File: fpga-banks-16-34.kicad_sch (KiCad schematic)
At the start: 25 parts, among them U1 ASFLMB-100.000MHZ-XY-T, U15 XC7K160T-FFG676, U8 PCA9517ADMR2G

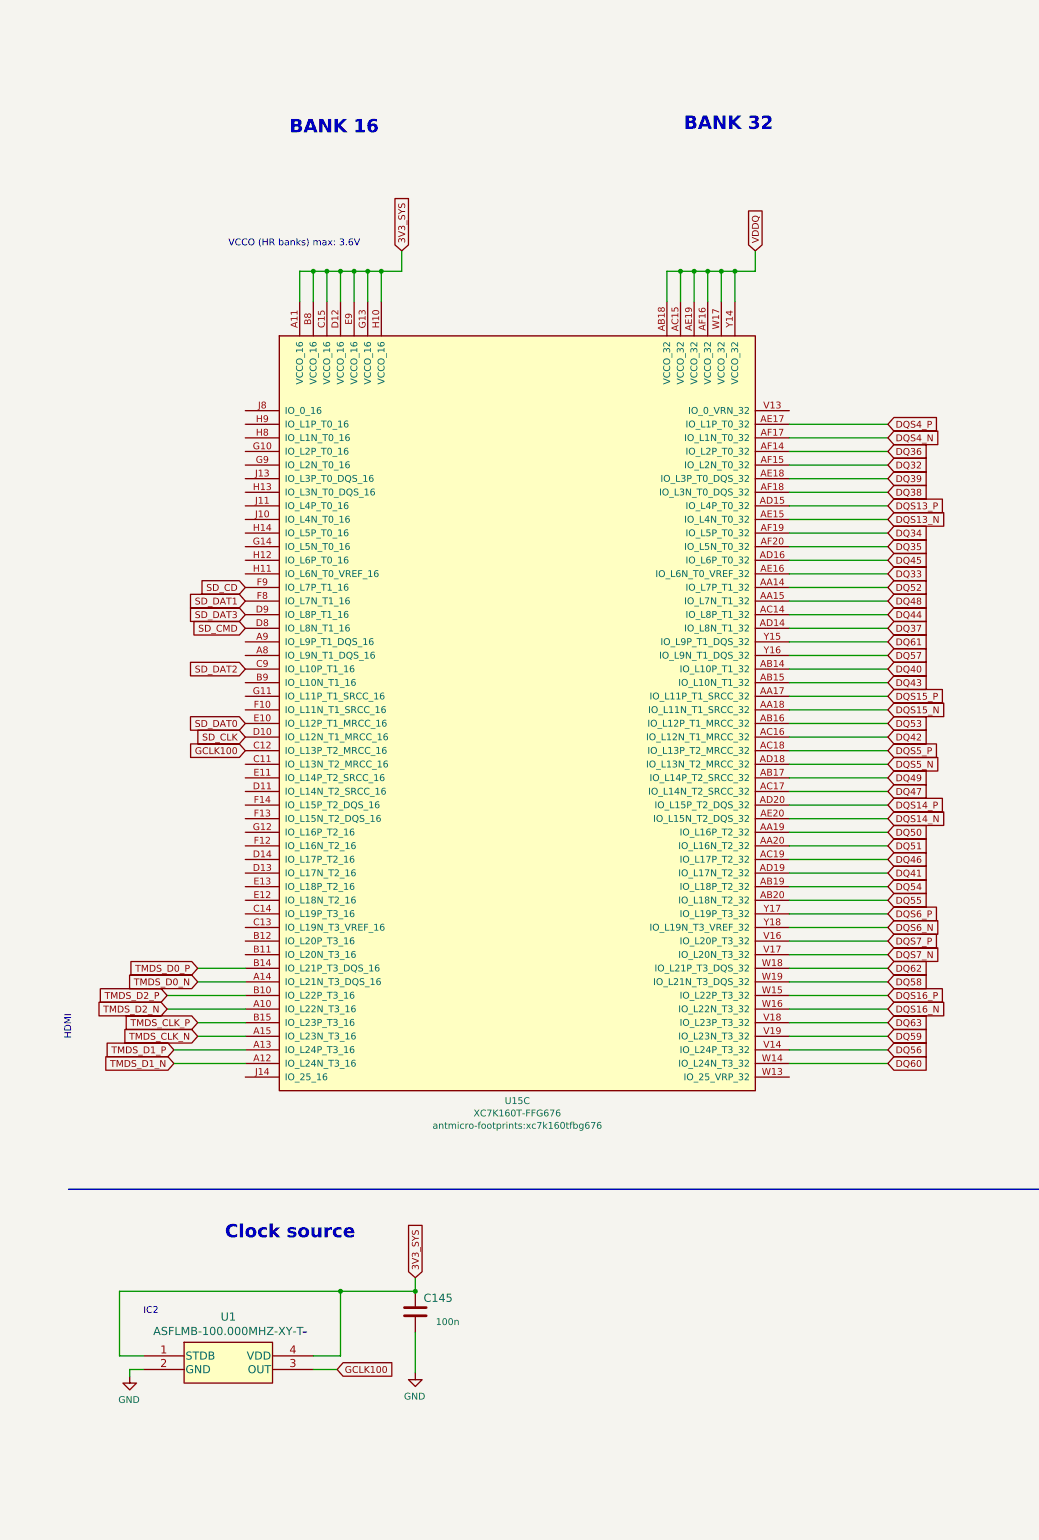
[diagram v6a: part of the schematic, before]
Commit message: Add missing FMC vias, route: MODE, JTAG, active discharge, reconnect 5V buses
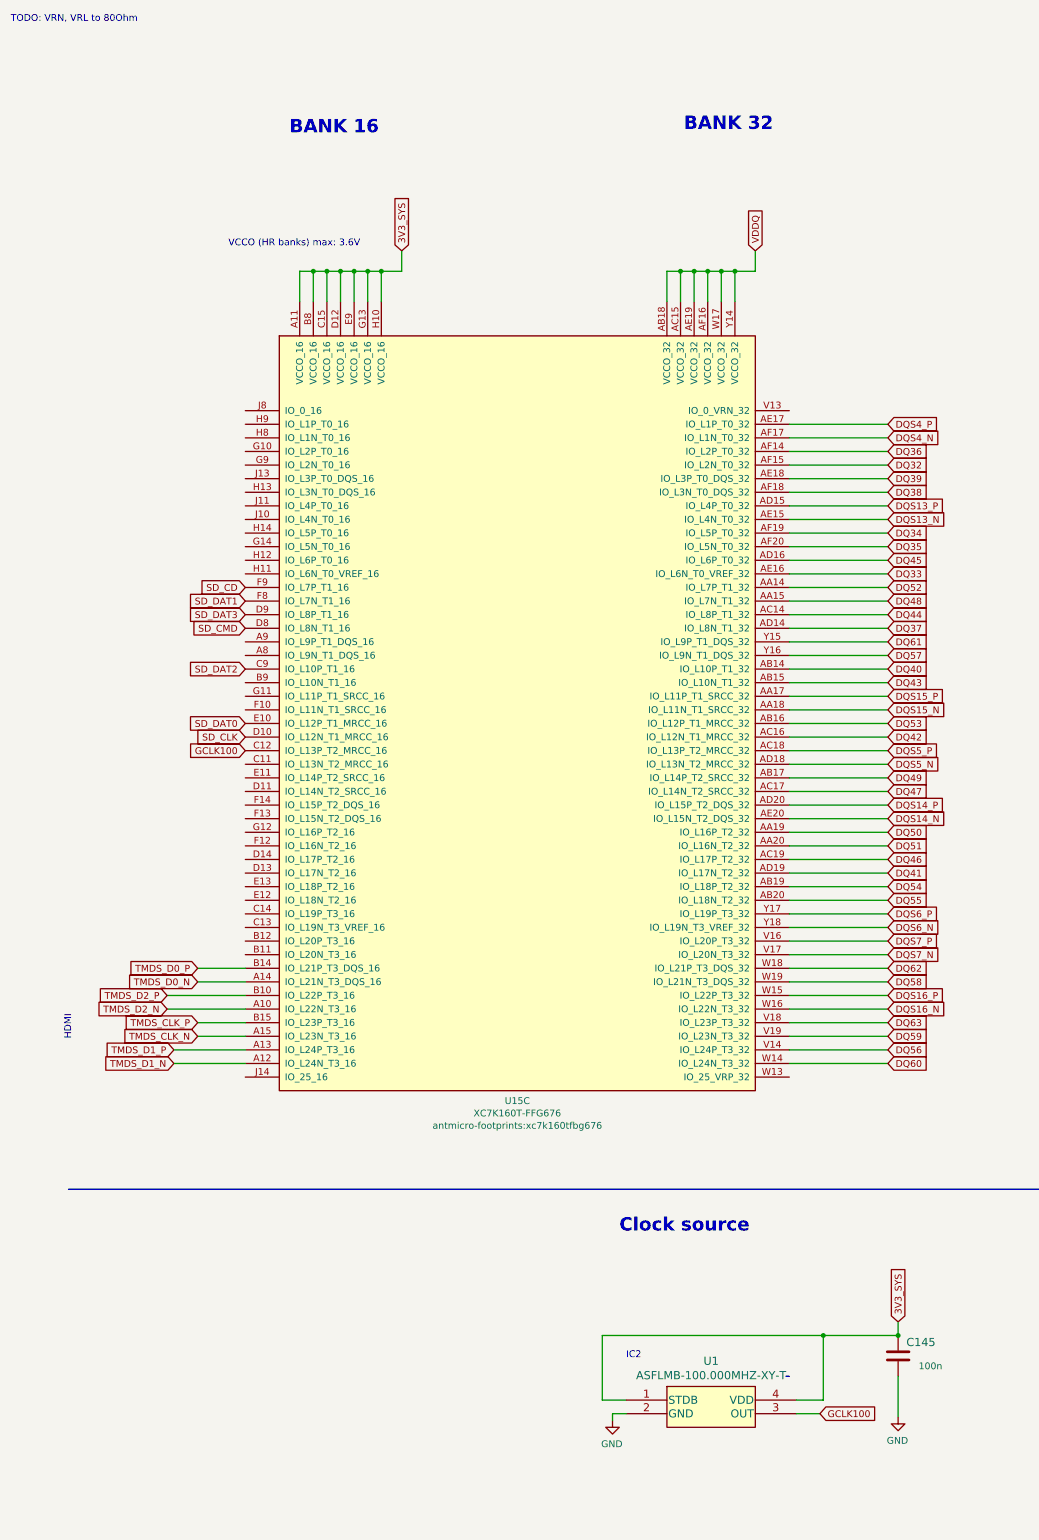
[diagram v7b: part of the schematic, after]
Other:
- note added: "TODO: VRN, VRL to 80Ohm"
- moved on the sheet: C145, U1
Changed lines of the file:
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@@
   (junction (at 60.96 50.165) (diameter 0) (color 0 0 0 0)
   )
-  (junction (at 77.47 240.665) (diameter 0) (color 0 0 0 0)
+  (junction (at 167.64 248.92) (diameter 0) (color 0 0 0 0)
   )
   (junction (at 278.13 262.89) (diameter 0) (color 0 0 0 0)
@@
   (junction (at 264.795 53.34) (diameter 0) (color 0 0 0 0)
   )
-  (junction (at 63.5 240.665) (diameter 0) (color 0 0 0 0)
+  (junction (at 153.67 248.92) (diameter 0) (color 0 0 0 0)
   )
   (junction (at 134.62 50.165) (diameter 0) (color 0 0 0 0)
@@
     (stroke (width 0) (type default) (color 0 0 0 0))
   )
-  (wire (pts (xy 58.42 255.27) (xy 62.865 255.27))
+  (wire (pts (xy 148.59 263.525) (xy 153.035 263.525))
     (stroke (width 0) (type default) (color 0 0 0 0))
   )
@@
     (stroke (width 0) (type default) (color 0 0 0 0))
   )
-  (wire (pts (xy 77.47 248.285) (xy 77.47 255.905))
+  (wire (pts (xy 167.64 256.54) (xy 167.64 264.16))
     (stroke (width 0) (type default) (color 0 0 0 0))
   )
@@
     (stroke (width 0) (type default) (color 0 0 0 0))
   )
-  (wire (pts (xy 22.225 240.665) (xy 63.5 240.665))
+  (wire (pts (xy 112.395 248.92) (xy 153.67 248.92))
     (stroke (width 0) (type default) (color 0 0 0 0))
   )
@@
     (stroke (width 0) (type default) (color 0 0 0 0))
   )
-  (wire (pts (xy 58.42 252.73) (xy 63.5 252.73))
+  (wire (pts (xy 148.59 260.985) (xy 153.67 260.985))
     (stroke (width 0) (type default) (color 0 0 0 0))
   )
-  (wire (pts (xy 26.67 255.27) (xy 24.13 255.27))
+  (wire (pts (xy 116.84 263.525) (xy 114.3 263.525))
     (stroke (width 0) (type default) (color 0 0 0 0))
   )
@@
     (stroke (width 0) (type default) (color 0 0 0 0))
   )
-  (wire (pts (xy 22.225 240.665) (xy 22.225 252.73))
+  (wire (pts (xy 112.395 248.92) (xy 112.395 260.985))
     (stroke (width 0) (type default) (color 0 0 0 0))
   )
@@
     (stroke (width 0) (type default) (color 0 0 0 0))
   )
-  (wire (pts (xy 24.13 255.27) (xy 24.13 256.54))
+  (wire (pts (xy 114.3 263.525) (xy 114.3 264.795))
     (stroke (width 0) (type default) (color 0 0 0 0))
   )
@@
     (stroke (width 0) (type default) (color 0 0 0 0))
   )
-  (wire (pts (xy 63.5 240.665) (xy 77.47 240.665))
+  (wire (pts (xy 153.67 248.92) (xy 167.64 248.92))
     (stroke (width 0) (type default) (color 0 0 0 0))
   )
@@
     (stroke (width 0) (type default) (color 0 0 0 0))
   )
-  (polyline (pts (xy 56.515 248.285) (xy 57.15 248.285))
+  (polyline (pts (xy 146.685 256.54) (xy 147.32 256.54))
     (stroke (width 0) (type default) (color 0 0 0 0))
   )
@@
     (stroke (width 0) (type default) (color 0 0 0 0))
   )
-  (wire (pts (xy 22.225 252.73) (xy 26.67 252.73))
+  (wire (pts (xy 112.395 260.985) (xy 116.84 260.985))
     (stroke (width 0) (type default) (color 0 0 0 0))
   )
@@
     (stroke (width 0) (type default) (color 0 0 0 0))
   )
-  (wire (pts (xy 77.47 240.665) (xy 77.47 238.125))
+  (wire (pts (xy 167.64 248.92) (xy 167.64 246.38))
     (stroke (width 0) (type default) (color 0 0 0 0))
   )
@@
     (stroke (width 0) (type default) (color 0 0 0 0))
   )
-  (wire (pts (xy 63.5 252.73) (xy 63.5 240.665))
+  (wire (pts (xy 153.67 260.985) (xy 153.67 248.92))
     (stroke (width 0) (type default) (color 0 0 0 0))
   )
@@
     (effects (font (size 2.4892 2.4892) (thickness 0.4978) bold) (justify left bottom))
   )
-  (text "Clock source" (at 41.91 231.14 0)
+  (text "Clock source" (at 115.57 229.87 0)
     (effects (font (size 2.4892 2.4892) (thickness 0.4978) bold) (justify left bottom))
   )
-  (text "IC2" (at 26.67 245.11 0)
+  (text "IC2" (at 116.84 253.365 0)
     (effects (font (size 1.27 1.27)) (justify left bottom))
   )
@@
     (effects (font (size 2.4892 2.4892) (thickness 0.4978) bold) (justify left bottom))
   )
+  (text "TODO: VRN, VRL to 80Ohm\n" (at 1.905 3.81 0)
+    (effects (font (size 1.27 1.27)) (justify left bottom))
+  )
   (global_label "DQ51" (shape input) (at 165.735 157.48 0) (fields_autoplaced)
     (effects (font (size 1.27 1.27)) (justify left))
@@
     )
   )
-  (global_label "3V3_SYS" (shape input) (at 77.47 238.125 90) (fields_autoplaced)
+  (global_label "3V3_SYS" (shape input) (at 167.64 246.38 90) (fields_autoplaced)
     (effects (font (size 1.27 1.27)) (justify left))
-    (property "Intersheet References" "${INTERSHEET_REFS}" (id 0) (at 0 0 0)
+    (property "Intersheet References" "${INTERSHEET_REFS}" (id 0) (at 90.17 8.255 0)
       (effects (font (size 1.27 1.27)) hide)
     )
@@
     )
   )
-  (global_label "GCLK100" (shape input) (at 62.865 255.27 0) (fields_autoplaced)
+  (global_label "GCLK100" (shape input) (at 153.035 263.525 0) (fields_autoplaced)
     (effects (font (size 1.27 1.27)) (justify left))
-    (property "Intersheet References" "${INTERSHEET_REFS}" (id 0) (at 0 0 0)
+    (property "Intersheet References" "${INTERSHEET_REFS}" (id 0) (at 90.17 8.255 0)
       (effects (font (size 1.27 1.27)) hide)
     )
@@
     (pin "2")
   )
-  (symbol (lib_id "data-center-dram-tester:GND") (at 24.13 256.54 0) (mirror y) (unit 1)
+  (symbol (lib_id "data-center-dram-tester:GND") (at 114.3 264.795 0) (mirror y) (unit 1)
     (in_bom yes) (on_board yes)
-    (property "Reference" "#PWR0141" (id 0) (at 24.13 262.89 0)
+    (property "Reference" "#PWR0141" (id 0) (at 114.3 271.145 0)
       (effects (font (size 1.27 1.27)) hide)
     )
-    (property "Value" "GND" (id 1) (at 24.003 260.9342 0))
-    (property "Footprint" "" (id 2) (at 24.13 256.54 0)
+    (property "Value" "GND" (id 1) (at 114.173 269.1892 0))
+    (property "Footprint" "" (id 2) (at 114.3 264.795 0)
       (effects (font (size 1.27 1.27)) hide)
     )
-    (property "Datasheet" "" (id 3) (at 24.13 256.54 0)
+    (property "Datasheet" "" (id 3) (at 114.3 264.795 0)
       (effects (font (size 1.27 1.27)) hide)
     )
     (pin "1")
   )
-  (symbol (lib_id "data-center-dram-tester:C_100n_0402_6V3") (at 77.47 244.475 0) (mirror y) (unit 1)
+  (symbol (lib_id "data-center-dram-tester:C_100n_0402_6V3") (at 167.64 252.73 0) (mirror y) (unit 1)
     (in_bom yes) (on_board yes)
-    (property "Reference" "C145" (id 0) (at 84.455 241.935 0)
+    (property "Reference" "C145" (id 0) (at 174.625 250.19 0)
       (effects (font (size 1.524 1.524)) (justify left))
     )
-    (property "Value" "C_100n_0402_6V3" (id 1) (at 77.47 248.285 0)
+    (property "Value" "C_100n_0402_6V3" (id 1) (at 167.64 256.54 0)
       (effects (font (size 1.524 1.524)) hide)
     )
-    (property "Footprint" "data-center-dram-tester-footprints:0402-cap" (id 2) (at 72.39 239.395 0)
+    (property "Footprint" "data-center-dram-tester-footprints:0402-cap" (id 2) (at 162.56 247.65 0)
       (effects (font (size 1.524 1.524)) (justify left) hide)
     )
-    (property "Datasheet" "" (id 3) (at 77.47 244.475 0)
+    (property "Datasheet" "" (id 3) (at 167.64 252.73 0)
       (effects (font (size 1.27 1.27)) hide)
     )
-    (property "Manufacturer" "Walsin" (id 4) (at 72.39 234.315 0)
+    (property "Manufacturer" "Walsin" (id 4) (at 162.56 242.57 0)
       (effects (font (size 1.524 1.524)) (justify left) hide)
     )
-    (property "MPN" "0402X104K6R3CT" (id 5) (at 72.39 236.855 0)
+    (property "MPN" "0402X104K6R3CT" (id 5) (at 162.56 245.11 0)
       (effects (font (size 1.524 1.524)) (justify left) hide)
     )
-    (property "Val" "100n" (id 6) (at 85.725 246.38 0)
+    (property "Val" "100n" (id 6) (at 175.895 254.635 0)
       (effects (font (size 1.27 1.27)) (justify left))
     )
@@
     (pin "2")
   )
-  (symbol (lib_id "data-center-dram-tester:GND") (at 77.47 255.905 0) (mirror y) (unit 1)
+  (symbol (lib_id "data-center-dram-tester:GND") (at 167.64 264.16 0) (mirror y) (unit 1)
     (in_bom yes) (on_board yes)
-    (property "Reference" "#PWR0142" (id 0) (at 77.47 262.255 0)
+    (property "Reference" "#PWR0142" (id 0) (at 167.64 270.51 0)
       (effects (font (size 1.27 1.27)) hide)
     )
-    (property "Value" "GND" (id 1) (at 77.343 260.2992 0))
-    (property "Footprint" "" (id 2) (at 77.47 255.905 0)
+    (property "Value" "GND" (id 1) (at 167.513 268.5542 0))
+    (property "Footprint" "" (id 2) (at 167.64 264.16 0)
       (effects (font (size 1.27 1.27)) hide)
     )
-    (property "Datasheet" "" (id 3) (at 77.47 255.905 0)
+    (property "Datasheet" "" (id 3) (at 167.64 264.16 0)
       (effects (font (size 1.27 1.27)) hide)
     )
     (pin "1")
   )
-  (symbol (lib_id "data-center-dram-tester:ASFLMB-100.000MHZ-XY-T") (at 26.67 252.73 0) (unit 1)
+  (symbol (lib_id "data-center-dram-tester:ASFLMB-100.000MHZ-XY-T") (at 116.84 260.985 0) (unit 1)
     (in_bom yes) (on_board yes)
-    (property "Reference" "U1" (id 0) (at 42.545 245.4402 0)
+    (property "Reference" "U1" (id 0) (at 132.715 253.6952 0)
       (effects (font (size 1.524 1.524)))
     )
-    (property "Value" "ASFLMB-100.000MHZ-XY-T" (id 1) (at 42.545 248.1326 0)
+    (property "Value" "ASFLMB-100.000MHZ-XY-T" (id 1) (at 132.715 256.3876 0)
       (effects (font (size 1.524 1.524)))
     )
-    (property "Footprint" "data-center-dram-tester-footprints:ASFLMB-100.000MHZ-XY-T" (id 2) (at 46.99 246.634 0)
+    (property "Footprint" "data-center-dram-tester-footprints:ASFLMB-100.000MHZ-XY-T" (id 2) (at 137.16 254.889 0)
       (effects (font (size 1.524 1.524)) hide)
     )
-    (property "Datasheet" "" (id 3) (at 26.67 252.73 0)
+    (property "Datasheet" "" (id 3) (at 116.84 260.985 0)
       (effects (font (size 1.524 1.524)))
     )
-    (property "MPN" "ASFLMB-100.000MHZ-XY-T" (id 4) (at 26.67 252.73 0)
+    (property "MPN" "ASFLMB-100.000MHZ-XY-T" (id 4) (at 116.84 260.985 0)
       (effects (font (size 1.27 1.27)) hide)
     )
-    (property "Manufacturer" "Abracon" (id 5) (at 26.67 252.73 0)
+    (property "Manufacturer" "Abracon" (id 5) (at 116.84 260.985 0)
       (effects (font (size 1.27 1.27)) hide)
     )

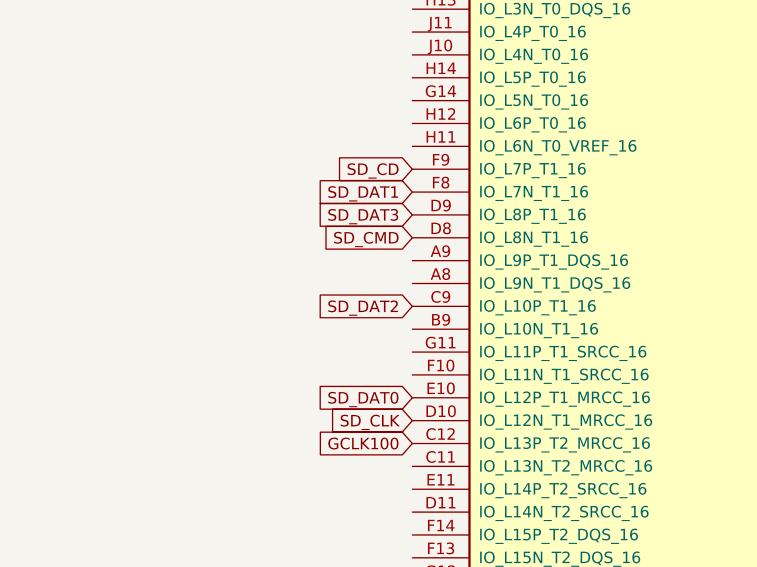
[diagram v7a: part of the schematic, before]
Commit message: Assign and connect misc. signals. Add, place and route decoupling capacitors
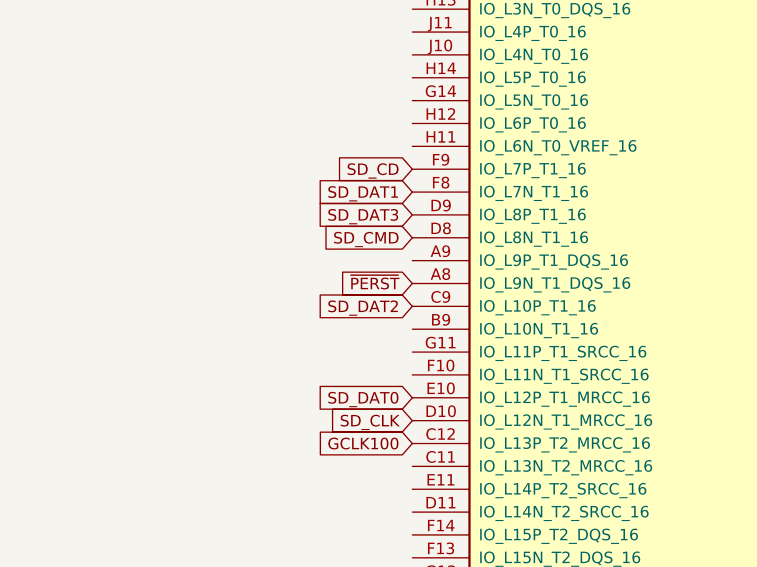
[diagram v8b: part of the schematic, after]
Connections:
- net ~{PERST}: now reaches U15.A8 (IO_L9N_T1_DQS_16)
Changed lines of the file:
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@@
+    )
+  )
+  (global_label "~{PERST}" (shape input) (at 45.72 121.92 180) (fields_autoplaced)
+    (effects (font (size 1.27 1.27)) (justify right))
+    (property "Intersheet References" "${INTERSHEET_REFS}" (id 0) (at 37.5296 121.8406 0)
+      (effects (font (size 1.27 1.27)) (justify right) hide)
     )
   )
